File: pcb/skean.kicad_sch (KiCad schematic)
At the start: 81 parts, among them J2 SWD, J3 USB-C Conn, J4 Conn_01x02_Female, K1 KEYSW, K10 KEYSW, K11 KEYSW, K12 KEYSW, K13 KEYSW, K14 KEYSW, K15 KEYSW, K16 KEYSW, K17 KEYSW, K18 KEYSW, K19 KEYSW, K2 KEYSW, K20 KEYSW, K21 KEYSW, K22 KEYSW, K3 KEYSW, K4 KEYSW, K5 KEYSW, K6 KEYSW, K7 KEYSW, K8 KEYSW, K9 KEYSW, Q2 AO3407, SW1 SW_SPDT, SW2 SW_SPDT, U1 E73-2G4M08S1E, U2 XC6220B331MR-G, U3 TP4054, U4 USBLC6-2SC6, X1 32.768kHz

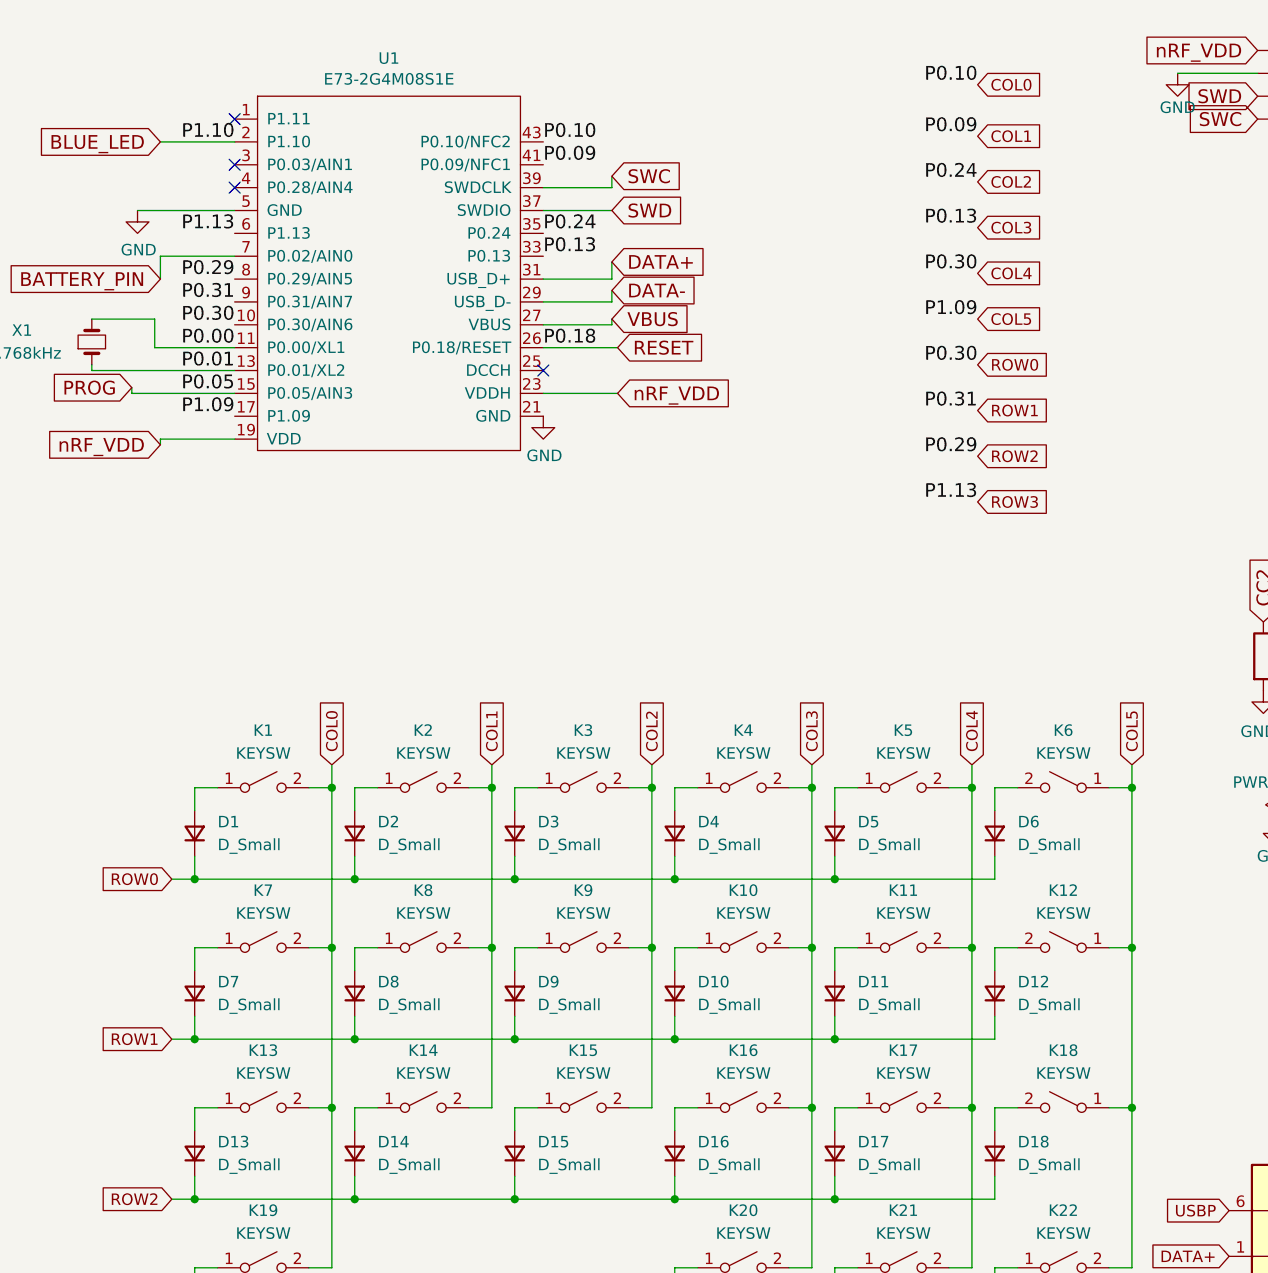
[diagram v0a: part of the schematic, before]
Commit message: Rev. 0.2: manual routing and pin fix
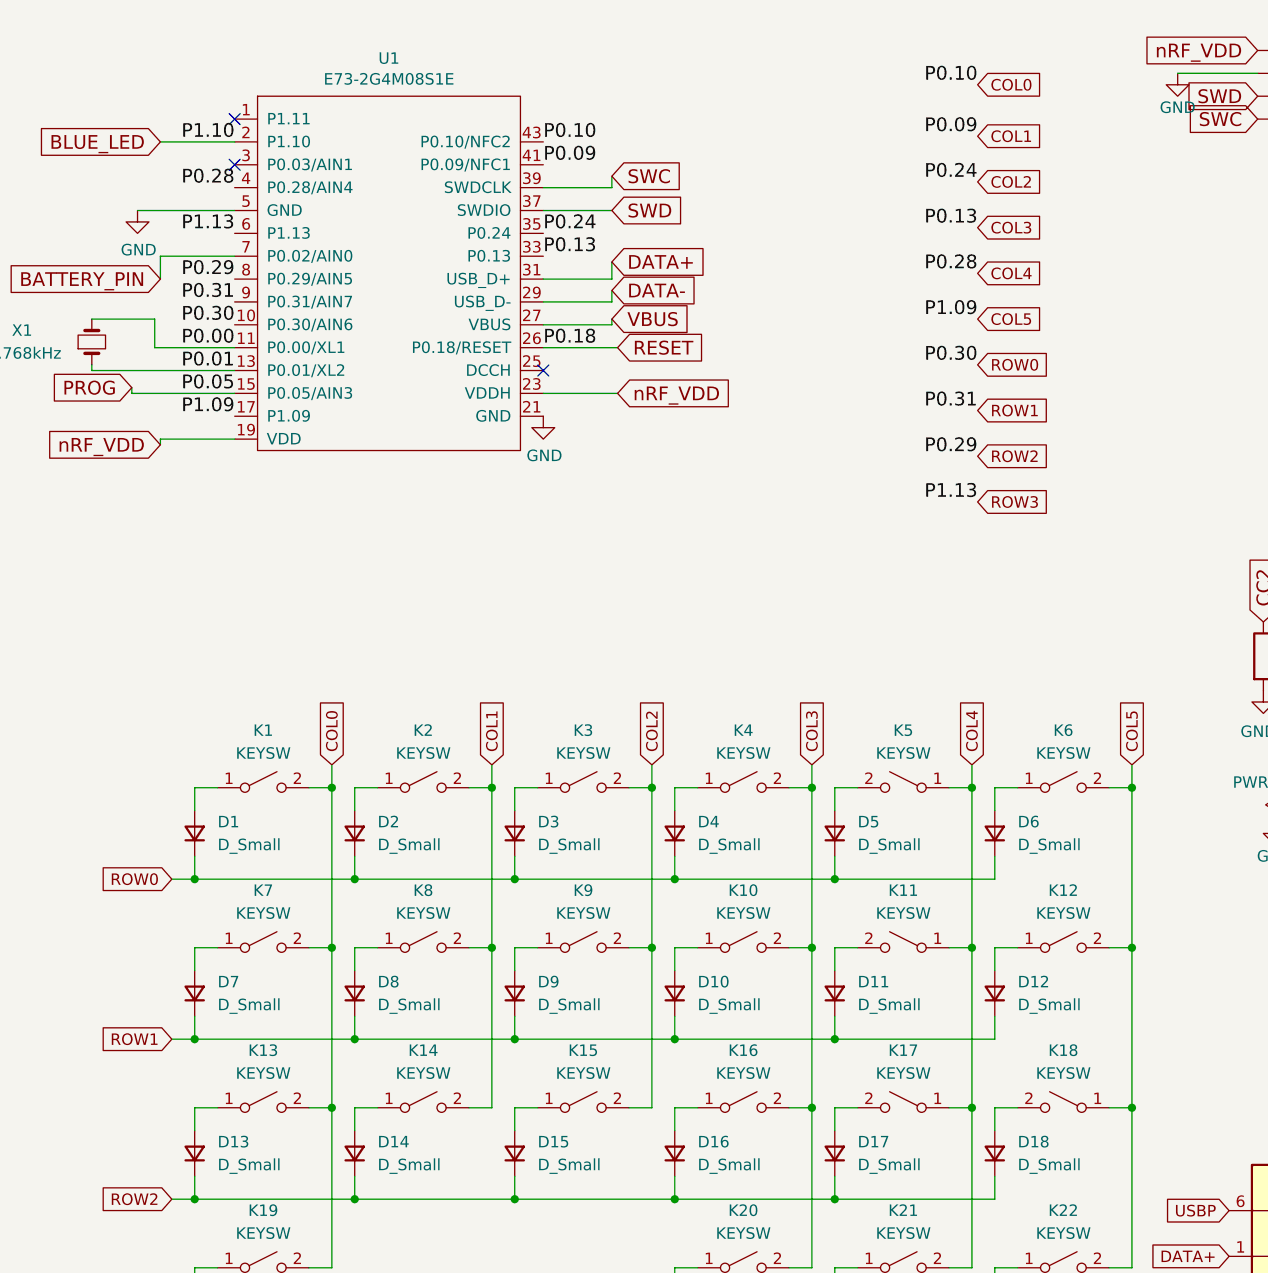
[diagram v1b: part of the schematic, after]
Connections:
- net COL4: now also K11.1 (A), K17.1 (A), K5.1 (A), U1.4 (P0.28/AIN4); no longer D1.1 (K), D2.1 (K), D3.1 (K), D4.1 (K), D5.1 (K), D6.1 (K), K11.2 (B), K17.2 (B), K5.2 (B), U1.10 (P0.30/AIN6)
- net COL5: now also K12.2 (B), K6.2 (B); no longer K12.1 (A), K6.1 (A)
- net at D11.2 (A): now also K11.2 (B); no longer K11.1 (A)
- net at D12.2 (A): now also K12.1 (A); no longer K12.2 (B)
- net at D17.2 (A): now also K17.2 (B); no longer K17.1 (A)
- net at D5.2 (A): now also K5.2 (B); no longer K5.1 (A)
- net at D6.2 (A): now also K6.1 (A); no longer K6.2 (B)
- new net ROW0: D1.1 (K), D2.1 (K), D3.1 (K), D4.1 (K), D5.1 (K), D6.1 (K), U1.10 (P0.30/AIN6)
- no-connect marks 8 -> 7
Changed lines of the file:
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@@
   (no_connect (at 59.055 23.495))
   (no_connect (at 59.055 28.575))
-  (no_connect (at 59.055 31.115))
   (no_connect (at 93.345 51.435))
   (no_connect (at 227.33 55.245))
@@
     (effects (font (size 1.524 1.524)) (justify right bottom))
   )
+  (label "P0.28" (at 59.055 31.115 180)
+    (effects (font (size 1.524 1.524)) (justify right bottom))
+  )
   (label "P1.13" (at 59.055 36.195 180)
     (effects (font (size 1.524 1.524)) (justify right bottom))
@@
     (effects (font (size 1.524 1.524)) (justify right bottom))
   )
-  (label "P0.30" (at 141.605 40.64 180)
+  (label "P0.28" (at 141.605 40.64 180)
     (effects (font (size 1.524 1.524)) (justify right bottom))
   )
@@
     (pin "2")
   )
-  (symbol (lib_id "Keyboard_Components:KEYSW") (at 133.35 97.79 0) (unit 1)
+  (symbol (lib_id "Keyboard_Components:KEYSW") (at 133.35 97.79 0) (mirror y) (unit 1)
     (in_bom yes) (on_board yes)
     (property "Reference" "K5" (id 0) (at 133.35 91.44 0))
@@
     (pin "2")
   )
-  (symbol (lib_id "Keyboard_Components:KEYSW") (at 133.35 115.57 0) (unit 1)
+  (symbol (lib_id "Keyboard_Components:KEYSW") (at 133.35 115.57 0) (mirror y) (unit 1)
     (in_bom yes) (on_board yes)
     (property "Reference" "K11" (id 0) (at 133.35 109.22 0))
@@
     (pin "2")
   )
-  (symbol (lib_id "Keyboard_Components:KEYSW") (at 133.35 133.35 0) (unit 1)
+  (symbol (lib_id "Keyboard_Components:KEYSW") (at 133.35 133.35 0) (mirror y) (unit 1)
     (in_bom yes) (on_board yes)
     (property "Reference" "K17" (id 0) (at 133.35 127 0))
@@
     (pin "2")
   )
-  (symbol (lib_id "Keyboard_Components:KEYSW") (at 151.13 97.79 0) (mirror y) (unit 1)
+  (symbol (lib_id "Keyboard_Components:KEYSW") (at 151.13 97.79 0) (unit 1)
     (in_bom yes) (on_board yes)
     (property "Reference" "K6" (id 0) (at 151.13 91.44 0))
@@
     (pin "2")
   )
-  (symbol (lib_id "Keyboard_Components:KEYSW") (at 151.13 115.57 0) (mirror y) (unit 1)
+  (symbol (lib_id "Keyboard_Components:KEYSW") (at 151.13 115.57 0) (unit 1)
     (in_bom yes) (on_board yes)
     (property "Reference" "K12" (id 0) (at 151.13 109.22 0))
